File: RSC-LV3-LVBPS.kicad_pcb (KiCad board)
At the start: 2 copper layers, 103 parts, among them J1 FTSH-105-01-L-DV-K-A, J2 USB_C_Receptacle_USB2.0_16P, J5 Conn_01x02, K1 Relay_SPST-NO, K3 Relay_SPST-NO, Q1 AO3400A, Q2 AO3400A, SW1 SW_SPST, U1 STM32G0B1CBTx, U2 ACS711xLCTR-12AB, U3 ACS711xLCTR-12AB, U4 TPS54302, U5 TLV74033PDBVR, U6 TJA1051T-3, Y1 Crystal_GND24, Y2 32.768 kHz 6pF

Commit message: more schematic work and initial layout
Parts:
- removed D17, D8: D_Schottky, Diode_SMD:D_SMA
- removed K1, K3: Relay_SPST-NO, Relay_THT:Relay_SPST_SANYOU_SRD_Series_Form_A
- added C28: 100u, Capacitor_THT:CP_Radial_D6.3mm_P2.50mm, F.Cu at (120.5, 123.0)
- added D18: D_Schottky, Diode_SMD:D_SOD-123F, F.Cu at (110.5, 108.5)
- added D19: D_Schottky, Diode_SMD:D_SOD-123F, F.Cu at (105.7, 132.9)
- added J3: Molex 43650-0500, Project_Library:Molex_Micro-Fit_3.0_43650-0500_1x05_P3.00mm_Horizontal_VerticalCompatible, F.Cu at (161.8, 90.6)
- added J4: Molex 43650-0500, Project_Library:Molex_Micro-Fit_3.0_43650-0500_1x05_P3.00mm_Horizontal_VerticalCompatible, F.Cu at (181.8, 90.6)
- added J6: Conn_01x02, Connector_Molex:Molex_Micro-Fit_3.0_43650-0200_1x02_P3.00mm_Horizontal, F.Cu at (123.0, 89.4)
- added K2: SANYOU_SRD_Form_A, Relay_THT:Relay_SPST_SANYOU_SRD_Series_Form_A, F.Cu at (120.5, 112.0)
- added K4: SANYOU_SRD_Form_A, Relay_THT:Relay_SPST_SANYOU_SRD_Series_Form_A, F.Cu at (109.2, 123.0)
- added R30: 33, Resistor_SMD:R_2512_6332Metric, F.Cu at (98.2, 136.2)
- added R31: 470, Resistor_SMD:R_0603_1608Metric_Pad0.98x0.95mm_HandSolder, F.Cu at (85.5, 136.7)
- added SW2: SLW-864587-2A-RA-N-D, SamacSys_Parts:SLW8645872ARAND, F.Cu at (57.5, 97.8)
- added U7: TLP175A, Package_SO:Toshiba_SOIC-4-6_4.4x3.6mm_P1.27mm, F.Cu at (91.5, 137.9)
- D16: footprint Diode_SMD:D_SMA -> Diode_SMD:D_SOD-123F
- SW1: value SW_SPST -> Molex 43650-0215; footprint Connector_Molex:Molex_Micro-Fit_3.0_43650-0215_1x02_P3.00mm_Vertical -> Connector_Molex:Molex_Micro-Fit_3.0_43650-0200_1x02_P3.00mm_Horizontal
- moved R24 182.1 mm to (18.0, 148.2)
- moved R25 182.1 mm to (18.0, 150.8)
- moved R26 182.1 mm to (18.0, 153.3)
- moved D13 177.6 mm to (22.0, 148.5)
- moved D14 177.6 mm to (22.0, 151.1)
- moved D15 177.6 mm to (22.0, 153.7)
- moved J5 163.2 mm to (27.8, 92.3)
- moved F1 148.1 mm to (40.7, 102.7), turned to 180 degrees
- moved D12 147.0 mm to (58.2, 130.3), turned to 180 degrees
- moved SW1 143.1 mm to (59.0, 92.0)
- moved R23 141.0 mm to (58.2, 134.0), turned to 180 degrees
- moved C20 135.4 mm to (65.2, 142.0), turned to 180 degrees
- moved C16 135.0 mm to (65.0, 128.8), turned to 180 degrees
- moved D11 134.0 mm to (66.5, 132.5), turned to 90 degrees
- moved D10 133.3 mm to (69.0, 132.5), turned to 90 degrees
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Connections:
- D16 pad 1: +5V -> +12V
- D16 pad 2: Net-(D16-A) -> +12V_LOCAL
- Q1 pad 3: Net-(D16-A) -> Net-(D18-A)

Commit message: more layout work
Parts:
- removed SW1: Molex 43650-0215, Connector_Molex:Molex_Micro-Fit_3.0_43650-0200_1x02_P3.00mm_Horizontal
- added C36: 1u, Capacitor_SMD:C_0603_1608Metric_Pad1.08x0.95mm_HandSolder, F.Cu at (190.6, 89.5)
- added J7: Conn_01x02, Connector_Molex:Molex_Micro-Fit_3.0_43650-0200_1x02_P3.00mm_Horizontal, F.Cu at (193.5, 100.7)
- added J8: Molex 43045-0400, Connector_Molex:Molex_Micro-Fit_3.0_43045-0400_2x02_P3.00mm_Horizontal, F.Cu at (217.5, 100.2)
- added Q3: AO3400A, Package_TO_SOT_SMD:SOT-23, F.Cu at (212.6, 87.4)
- added R32: 10k, Resistor_SMD:R_0603_1608Metric_Pad0.98x0.95mm_HandSolder, F.Cu at (192.6, 86.5)
- added R33: 1k, Resistor_SMD:R_0603_1608Metric_Pad0.98x0.95mm_HandSolder, F.Cu at (192.6, 88.0)
- added R34: 5.1k, Resistor_SMD:R_0603_1608Metric_Pad0.98x0.95mm_HandSolder, F.Cu at (212.6, 84.2)
- moved D4 221.6 mm to (246.9, 84.1), turned to 90 degrees
- moved J5 218.4 mm to (246.0, 100.7), turned to 180 degrees
- moved C9 217.7 mm to (244.9, 84.1), turned to 90 degrees
- moved R13 214.2 mm to (243.2, 84.1), turned to 90 degrees
- moved R12 213.4 mm to (243.2, 87.6), turned to 90 degrees
- moved U6 194.3 mm to (62.4, 78.5), turned to -90 degrees
- moved C21 191.2 mm to (58.9, 79.9), turned to 90 degrees
- moved R21 190.3 mm to (240.8, 59.9), turned to -90 degrees
- moved R20 190.2 mm to (238.0, 58.6), turned to 0 degrees
- moved D16 189.3 mm to (246.5, 63.9), turned to 0 degrees
- moved R27 189.2 mm to (60.9, 85.5), turned to 180 degrees
- moved C23 187.9 mm to (62.4, 72.0)
- moved C22 187.8 mm to (62.4, 73.8)
- moved C13 185.6 mm to (242.5, 64.6), turned to -90 degrees
- moved C15 185.5 mm to (235.0, 60.9), turned to -90 degrees
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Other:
- board outline added: 210 x 60 mm
- board text added: "BOOT"
- board text added: "NRST"
- board text added: "USR"

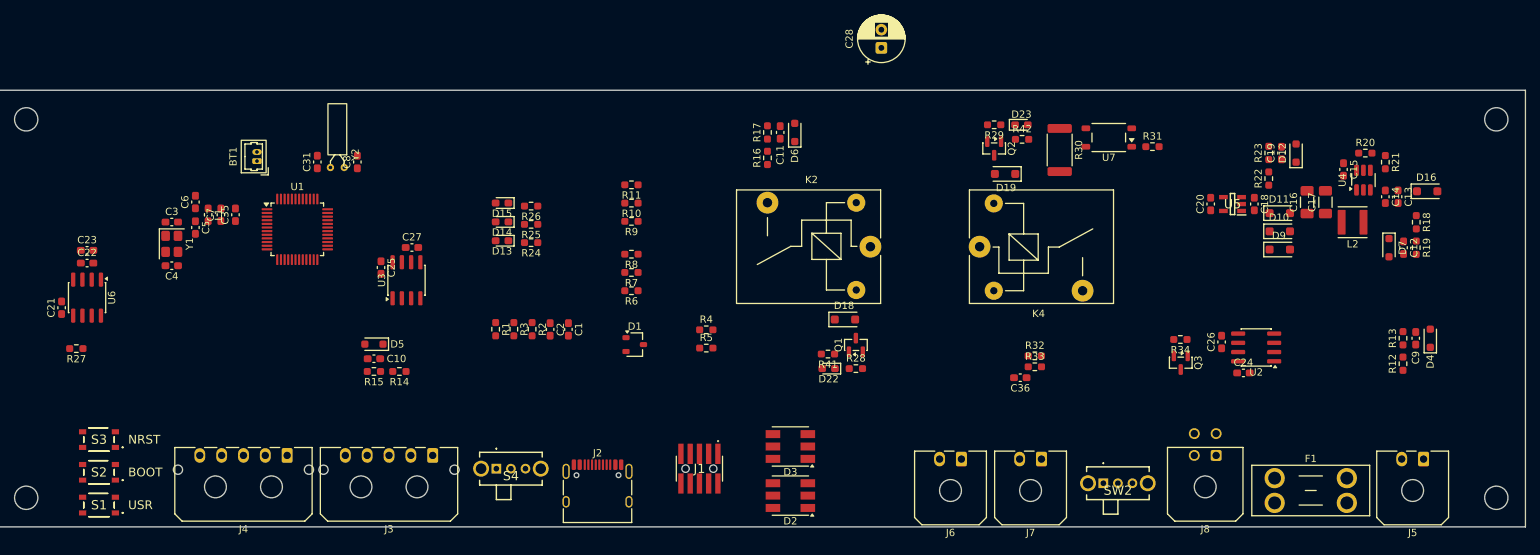
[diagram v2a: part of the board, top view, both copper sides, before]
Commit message: schematic changes and initial routing
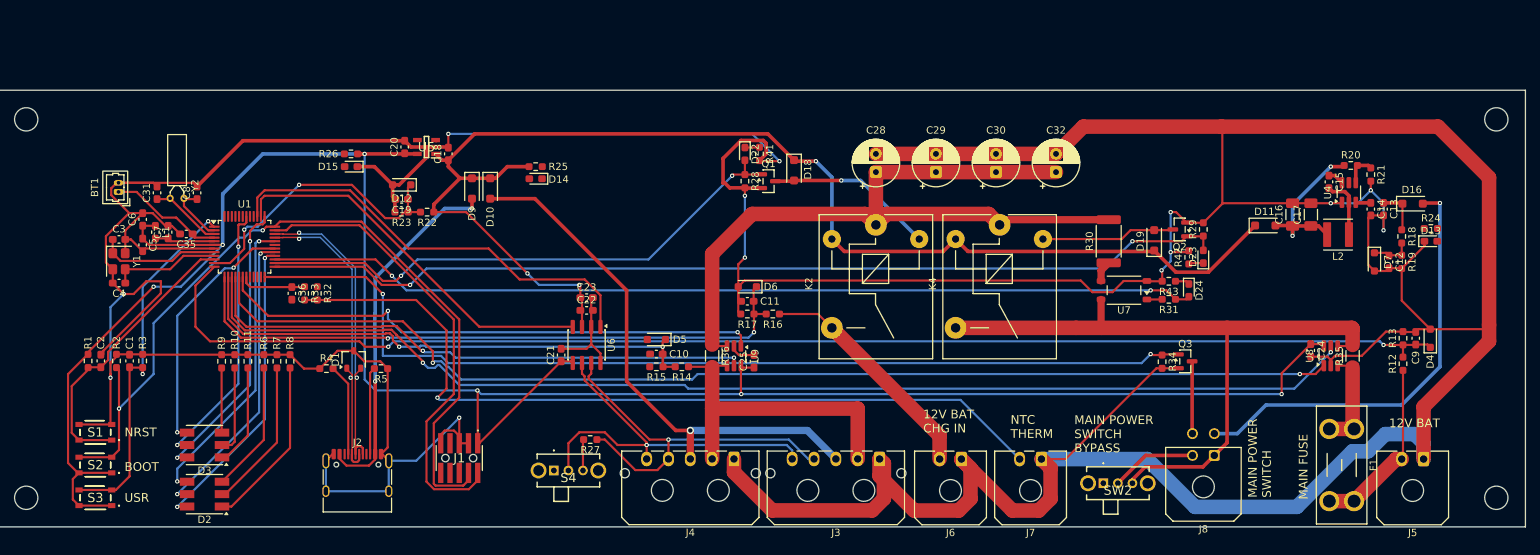
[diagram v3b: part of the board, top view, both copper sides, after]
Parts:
- removed C26, C27: 1n, Capacitor_SMD:C_0603_1608Metric_Pad1.08x0.95mm_HandSolder
- removed U2, U3: ACS711xLCTR-12AB, Package_SO:SOIC-8_3.9x4.9mm_P1.27mm
- added C29: 100u, Capacitor_THT:CP_Radial_D6.3mm_P2.50mm, F.Cu at (179.0, 61.2)
- added C30: 100u, Capacitor_THT:CP_Radial_D6.3mm_P2.50mm, F.Cu at (187.2, 61.2)
- added C32: 100u, Capacitor_THT:CP_Radial_D6.3mm_P2.50mm, F.Cu at (195.5, 61.2)
- added D24: LED, LED_SMD:LED_0603_1608Metric_Pad1.05x0.95mm_HandSolder, F.Cu at (213.8, 77.5)
- added R35: 2m, Resistor_SMD:R_1206_3216Metric_Pad1.30x1.75mm_HandSolder, F.Cu at (236.2, 86.5)
- added R36: 2m, Resistor_SMD:R_1206_3216Metric_Pad1.30x1.75mm_HandSolder, F.Cu at (148.2, 86.5)
- added R43: 470, Resistor_SMD:R_0603_1608Metric_Pad0.98x0.95mm_HandSolder, F.Cu at (211.0, 76.2)
- added U8: INA181A2, Package_TO_SOT_SMD:SOT-23-6_Handsoldering, F.Cu at (233.2, 86.5)
- added U9: INA181A2, Package_TO_SOT_SMD:SOT-23-6_Handsoldering, F.Cu at (151.2, 86.5)
- moved D13 127.6 mm to (247.0, 70.8), turned to 0 degrees
- moved R24 123.6 mm to (247.0, 69.0), turned to 0 degrees
- moved D12 123.0 mm to (105.6, 63.0), turned to 180 degrees
- moved C19 121.1 mm to (105.6, 65.0), turned to 180 degrees
- moved R23 119.4 mm to (105.6, 66.8), turned to 180 degrees
- moved R22 115.7 mm to (109.1, 66.8), turned to 180 degrees
- moved D9 111.3 mm to (115.2, 63.5), turned to -90 degrees
- moved C20 111.0 mm to (106.0, 57.8)
- moved U5 111.0 mm to (109.0, 57.8)
- moved C18 111.0 mm to (112.0, 58.8), turned to 90 degrees
- moved D10 108.7 mm to (117.8, 63.5), turned to -90 degrees
- moved R33 100.8 mm to (92.2, 77.9), turned to -90 degrees
- moved C36 100.8 mm to (90.5, 77.9), turned to -90 degrees
- moved R32 99.0 mm to (94.0, 77.9), turned to -90 degrees
- moved D2 80.5 mm to (78.5, 105.5)
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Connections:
- U1 pad 15: I_SENSE_BAT -> INA_REF_BAT
- U1 pad 16: I_SENSE_LOAD -> INA_REF_LOAD
- U1 pad 17: unconnected-(U1-PA6-Pad17) -> I_SENSE_BAT
- U1 pad 18: unconnected-(U1-PA7-Pad18) -> I_SENSE_LOAD
- U1 pad 19: RELAY_CONTROL_BAT -> THERMISTOR_SENSE
- U1 pad 20: RELAY_CONTROL_DCDC -> unconnected-(U1-PB1-Pad20)
- U1 pad 24: unconnected-(U1-PB12-Pad24) -> POWER_SWITCH_LED
- U1 pad 25: unconnected-(U1-PB13-Pad25) -> RELAY_CONTROL_BAT
- U1 pad 26: unconnected-(U1-PB14-Pad26) -> RELAY_CONTROL_DCDC
- U1 pad 27: unconnected-(U1-PB15-Pad27) -> PRECHARGE_CONTROL_BAT
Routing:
- net GND: track 0.00 -> 841.2 mm, vias 0 -> 13
- net +3.3V: track 0.00 -> 309.3 mm, vias 0 -> 6
- net V_SENSE_12_BAT: track 0.00 -> 182.5 mm, vias 0 -> 2
- net +5V: track 0.00 -> 181.1 mm, vias 0 -> 3
- net INA_REF_BAT: track 0.00 -> 164.1 mm, vias 0 -> 2
- net I_SENSE_BAT: track 0.00 -> 158.9 mm, vias 0 -> 2
- net POWER_SWITCH_LED: track 0.00 -> 136.1 mm, vias 0 -> 2
- net RELAY_CONTROL_BAT: track 0.00 -> 133.4 mm, vias 0 -> 2
- net PRECHARGE_CONTROL_BAT: track 0.00 -> 128.0 mm, vias 0 -> 2
- net BOOT0: track 0.00 -> 114.7 mm, vias 0 -> 2
- net Net-(J7-Pin_2): track 0.00 -> 114.5 mm, vias 0 -> 1
- net /Current Sense (LOAD)/IN: track 0.00 -> 105.5 mm
- net /Current Sense (BAT)/OUT: track 0.00 -> 94.3 mm
- net V_SENSE_12_DCDC: track 0.00 -> 88.3 mm, vias 0 -> 2
- net INA_REF_LOAD: track 0.00 -> 77.4 mm, vias 0 -> 2
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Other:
- board text added: "12V BAT"
- board text added: "12V BAT CHG IN"
- board text added: "MAIN FUSE"
- board text added: "MAIN POWER SWITCH"
- board text added: "MAIN POWER SWITCH BYPASS"
- board text added: "NTC THERM"
